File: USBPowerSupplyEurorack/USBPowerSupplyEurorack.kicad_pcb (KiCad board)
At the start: 2 copper layers, 9.8 x 110 mm, 23 parts, among them J1 1734366-1, J2 10129381-910001BLF, Q1 Q_PMOS_GSD, T1 RS6-0512D

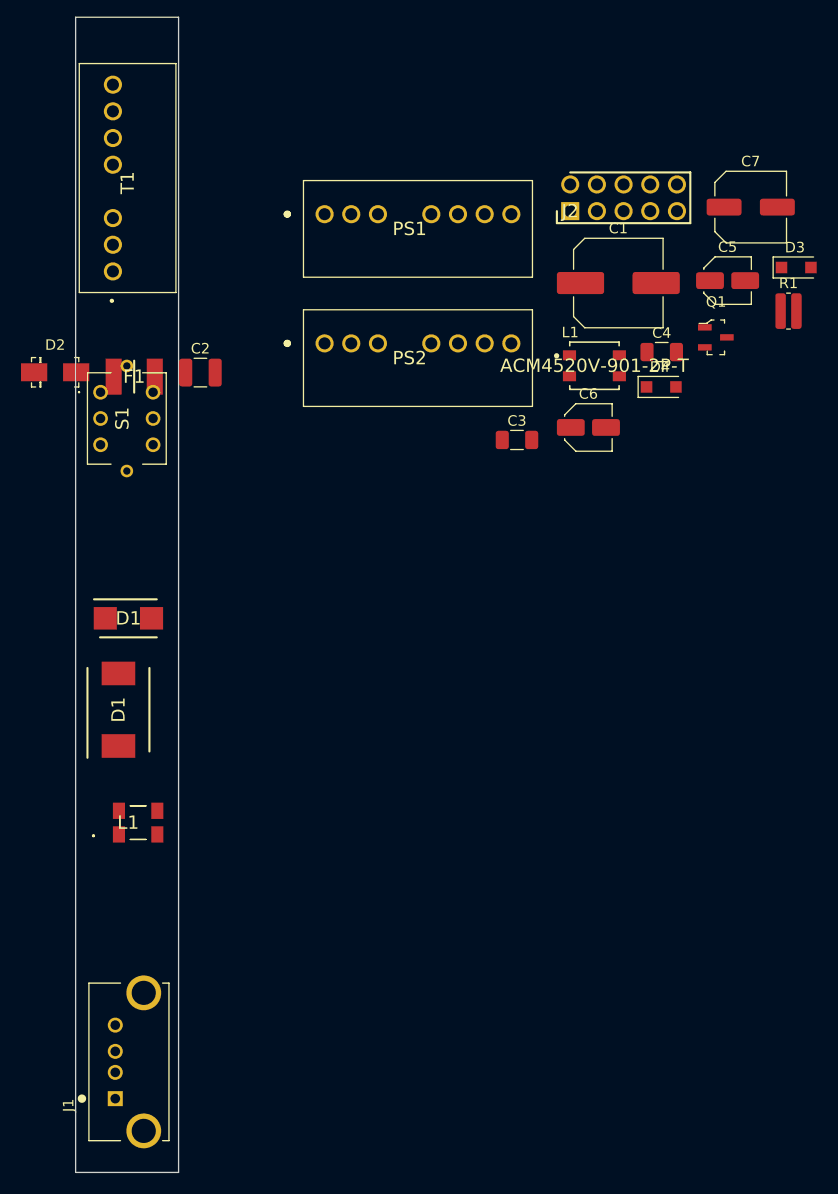
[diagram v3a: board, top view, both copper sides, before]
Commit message: updated all footprints in pcbnew
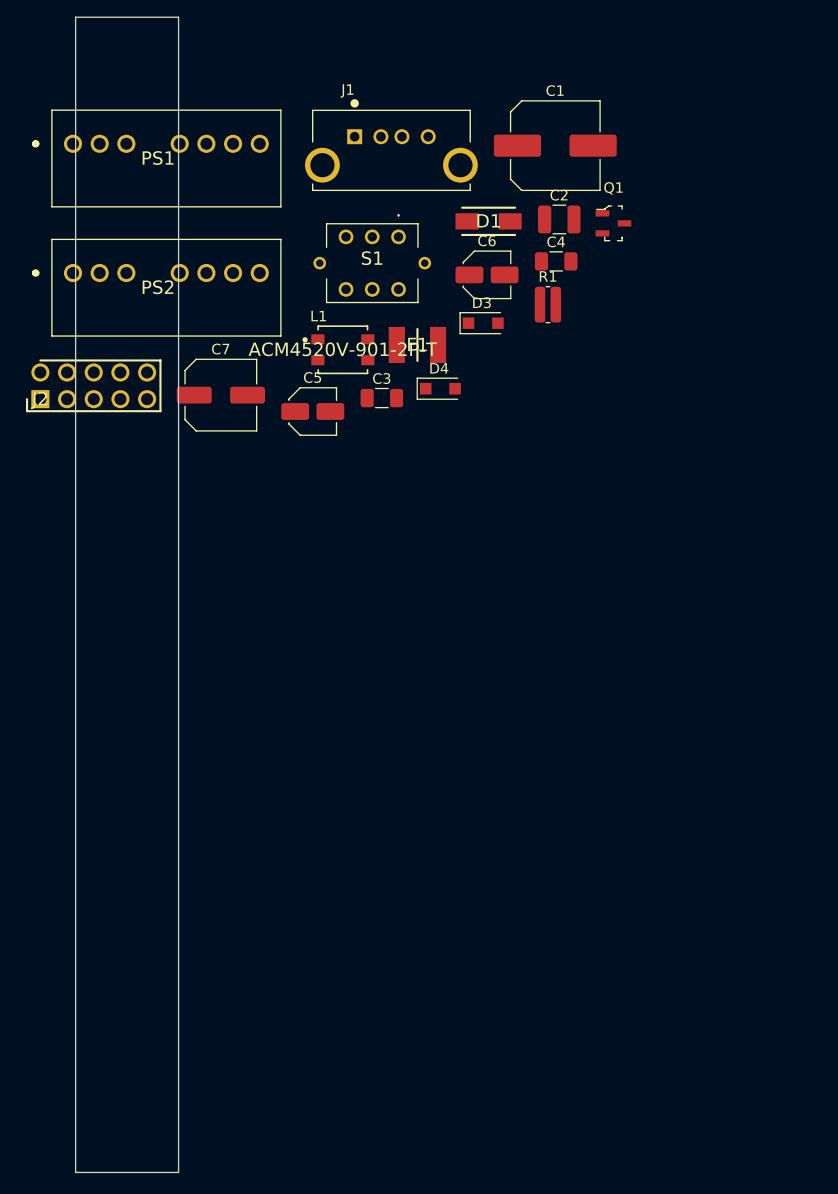
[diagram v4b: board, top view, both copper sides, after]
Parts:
- removed the D1 at (139.6, 105.3)
- removed the D1 at (138.6, 114.0)
- removed D2: SMAJ5.0CA, digikey-footprints:DO-214AC
- removed the L1 at (183.9, 81.3)
- removed the L1 at (140.5, 124.8)
- removed T1: RS6-0512D, RS6-0512D:RS60505S
- added D1: SMAJ5.0CA, DIONM5026X229N, F.Cu at (173.9, 67.6)
- added L1: ACM4520V-901-2P-T, eec2:TDK-ACM4520V-901-2P-T-0, F.Cu at (160.0, 79.8)
- moved J1 94.4 mm to (161.1, 59.5), turned to 0 degrees
- moved C7 53.5 mm to (148.4, 84.1)
- moved J2 53.5 mm to (131.2, 84.5)
- moved C5 41.4 mm to (157.1, 85.7)
- moved C2 37.1 mm to (180.6, 67.4)
- moved S1 32.0 mm to (165.3, 69.0), turned to 0 degrees
- moved D3 30.3 mm to (173.4, 77.3)
- moved F1 27.1 mm to (167.1, 79.3)
- moved PS1 24.9 mm to (134.3, 60.2)
- moved PS2 24.9 mm to (134.3, 72.5)
- moved R1 22.9 mm to (179.5, 75.5)
- moved D4 21.0 mm to (169.3, 83.5)
- moved C6 17.4 mm to (173.7, 72.7)
- moved Q1 14.6 mm to (185.8, 67.8)
- moved C1 14.4 mm to (180.2, 60.4)
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
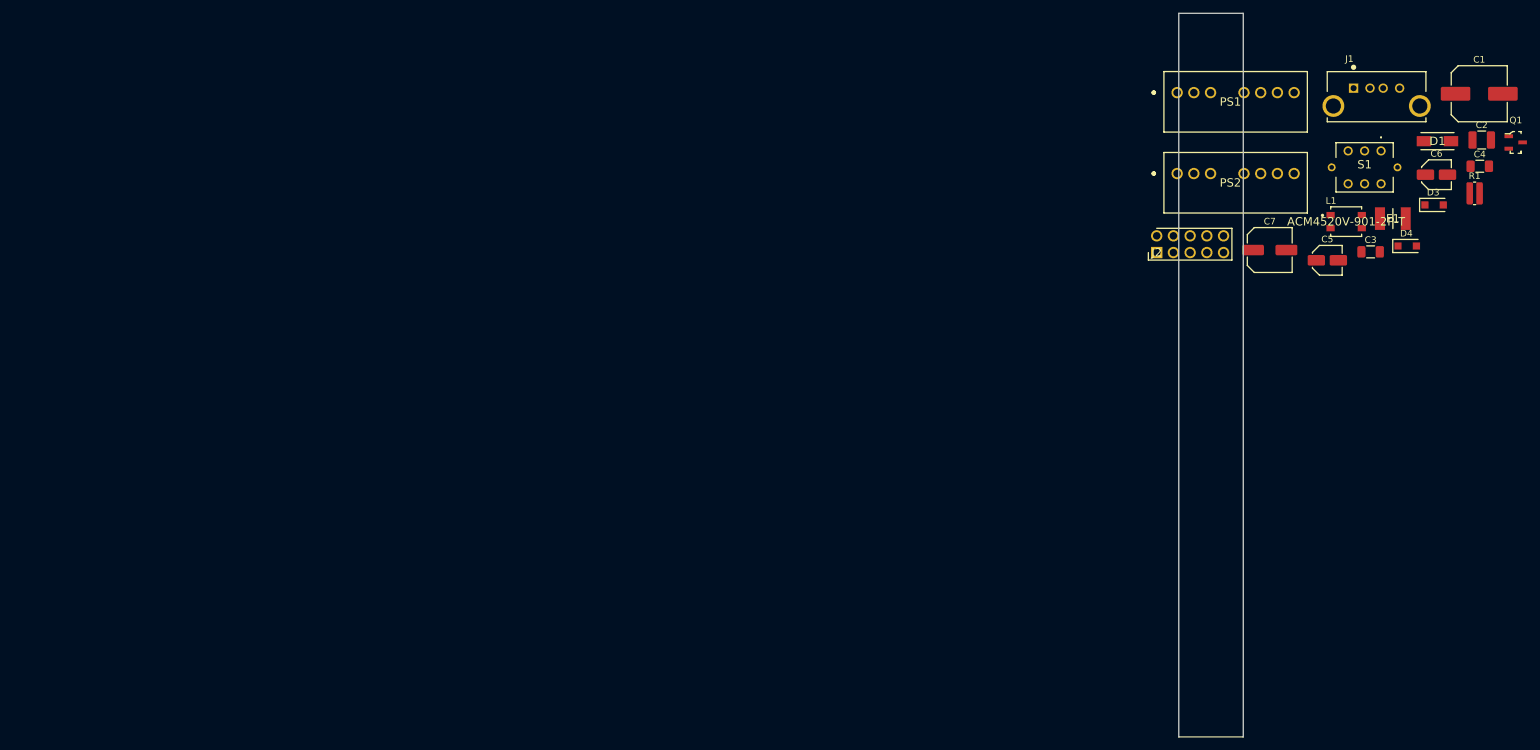
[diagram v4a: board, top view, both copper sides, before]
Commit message: placed components on the PCB
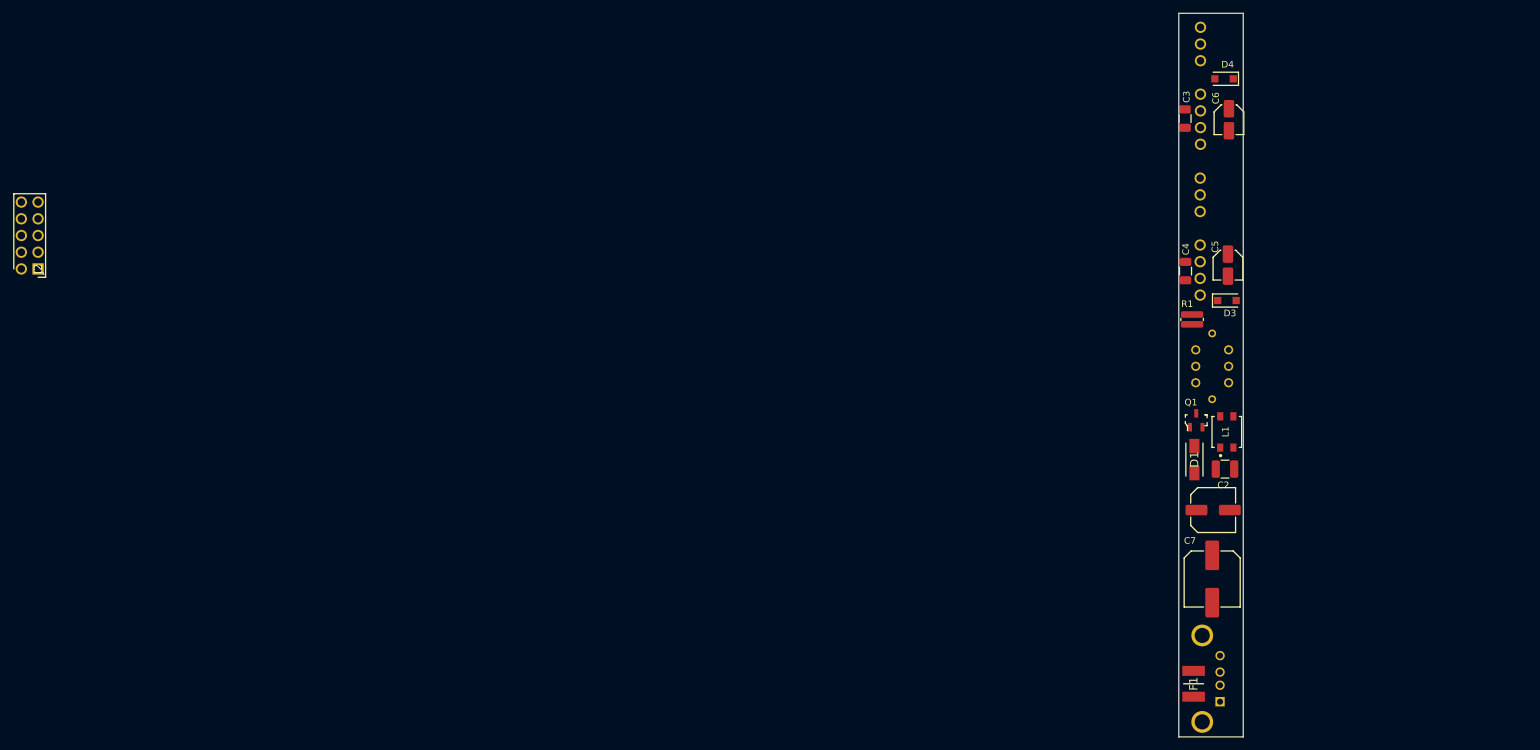
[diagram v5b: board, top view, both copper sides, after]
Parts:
- J1, PS1, PS2, S1: moved to B.Cu
- moved J2 170.0 mm to (-38.8, 87.0), turned to 90 degrees
- moved J1 95.4 mm to (140.8, 152.8), turned to 90 degrees
- moved C1 84.2 mm to (139.6, 134.1), turned to 270 degrees
- moved F1 76.9 mm to (136.8, 150.0), turned to 90 degrees
- moved Q1 64.3 mm to (137.2, 110.0), turned to 90 degrees
- moved C2 63.4 mm to (141.6, 117.4)
- moved D1 60.9 mm to (136.9, 116.0), turned to 90 degrees
- moved C4 47.5 mm to (135.6, 87.3), turned to 270 degrees
- moved R1 47.0 mm to (136.6, 94.7), turned to 90 degrees
- moved S1 45.1 mm to (137.1, 104.3), turned to 270 degrees
- moved C7 40.4 mm to (139.8, 123.6)
- moved D4 37.7 mm to (141.4, 58.1), turned to 180 degrees
- moved L1 36.8 mm to (141.8, 111.8), turned to 90 degrees
- moved C3 34.7 mm to (135.5, 64.1), turned to 270 degrees
- moved D3 34.7 mm to (141.9, 91.8)
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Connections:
- C1 pad 2: +5V -> GND
- C2 pad 2: +5V -> GND
- C7 pad 2: +5V -> GND
- D1 pad 2: +5V -> GND
- J1 pad 4: +5V -> GND
- L1 pad 2: +5V -> GND
- Q1 pad 1: +5V -> GND

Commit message: routing test for price evaluation
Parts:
- moved D4 12.0 mm to (141.9, 70.1)
- moved F1 1.38 mm to (136.8, 148.7)
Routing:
- net GND: track 0.00 -> 47.8 mm
- net +5VD: track 0.00 -> 46.4 mm
- net 0V: track 0.00 -> 27.0 mm
- net Net-(C1-Pad1): track 0.00 -> 24.9 mm
- net Net-(J1-PadSH1): track 0.00 -> 18.0 mm
- net -12V: track 0.00 -> 10.7 mm
- net +5V: track 0.00 -> 10.0 mm
- net +12V: track 0.00 -> 6.94 mm
- net Net-(F1-Pad1): track 0.00 -> 4.86 mm
- net Net-(R1-Pad1): track 0.00 -> 3.62 mm

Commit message: finished updating footprints, edited TVS diode's footprint
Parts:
- removed L1: ACM4520V-901-2P-T, eec2:TDK-ACM4520V-901-2P-T-0
- added FL1: ACP3225-102-2P-T000, ACP3225-102-2P-T000:ACP3225, F.Cu at (184.5, 85.4)
- C1: footprint Capacitor_SMD:C_Elec_8x10.2 -> Capacitor_SMD:C_Elec_6.3x7.7
- C2: value 22uFMLCC -> 22uF; footprint Capacitor_SMD:C_1210_3225Metric -> Capacitor_SMD:C_0805_2012Metric
- C3, C4: value 100nF MLCC -> 100nF; footprint Capacitor_SMD:C_1206_3216Metric -> Capacitor_SMD:C_0402_1005Metric
- C5, C6: value 1uF -> 4.7uF
- C7: footprint Capacitor_SMD:C_Elec_6.3x5.8 -> Capacitor_SMD:C_Elec_5x5.4
- D1: footprint DIONM5026X229N -> digikey-footprints:DO-214AC-BIPOLAR
- D3, D4: value 1N4004 -> 1N4007
- F1: footprint 1812L110_16DR:FUSC4632X125N -> Fuse:Fuse_1812_4532Metric
- J1, PS1, PS2, S1: moved to F.Cu
- R1: value 510 -> 1.5K; footprint Resistor_SMD:R_0612_1632Metric -> Resistor_SMD:R_0805_2012Metric
- moved J2 192.1 mm to (153.2, 86.3), turned to 0 degrees
- moved J1 100.8 mm to (183.2, 61.3), turned to 0 degrees
- moved F1 85.5 mm to (189.2, 81.1), turned to 0 degrees
- moved Q1 75.4 mm to (201.9, 71.2), turned to 0 degrees
- moved C3 71.0 mm to (206.5, 66.3), turned to 0 degrees
- moved D1 67.5 mm to (201.2, 95.5), turned to 0 degrees
- moved C2 66.4 mm to (194.9, 77.8)
- moved C4 64.6 mm to (198.9, 74.6), turned to 0 degrees
- moved D4 60.5 mm to (202.3, 67.0), turned to 0 degrees
- moved S1 60.3 mm to (187.3, 70.8), turned to 0 degrees
- moved C1 59.0 mm to (183.7, 94.9), turned to 0 degrees
- moved C5 56.2 mm to (195.8, 70.1), turned to 0 degrees
- moved D3 55.6 mm to (194.8, 74.7)
- moved R1 53.3 mm to (189.0, 85.0), turned to 0 degrees
- moved C7 48.7 mm to (169.7, 85.2)
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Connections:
- C3 pad 1: 0V -> +12V
- C3 pad 2: -12V -> 0V
- C4 pad 1: +12V -> 0V
- C4 pad 2: 0V -> -12V
- F1 pad 2: +5VD -> +5V
- PS1 pad 3: Net-(PS1-Pad3) -> CTRL
- PS2 pad 3: Net-(PS2-Pad3) -> CTRL
- S1 pad 1: +5VD -> CTRL
- S1 pad 2: +5VD -> CTRL
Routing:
- net GND: track 47.8 -> 0.00 mm
- net +5VD: track 46.4 -> 0.00 mm
- net 0V: track 27.0 -> 0.00 mm
- net Net-(C1-Pad1): track 24.9 -> 0.00 mm
- net Net-(J1-PadSH1): track 18.0 -> 0.00 mm
- net -12V: track 10.7 -> 0.00 mm
- net +5V: track 10.0 -> 0.00 mm
- net +12V: track 6.94 -> 0.00 mm
- net Net-(F1-Pad1): track 4.86 -> 0.00 mm
- net Net-(R1-Pad1): track 3.62 -> 0.00 mm

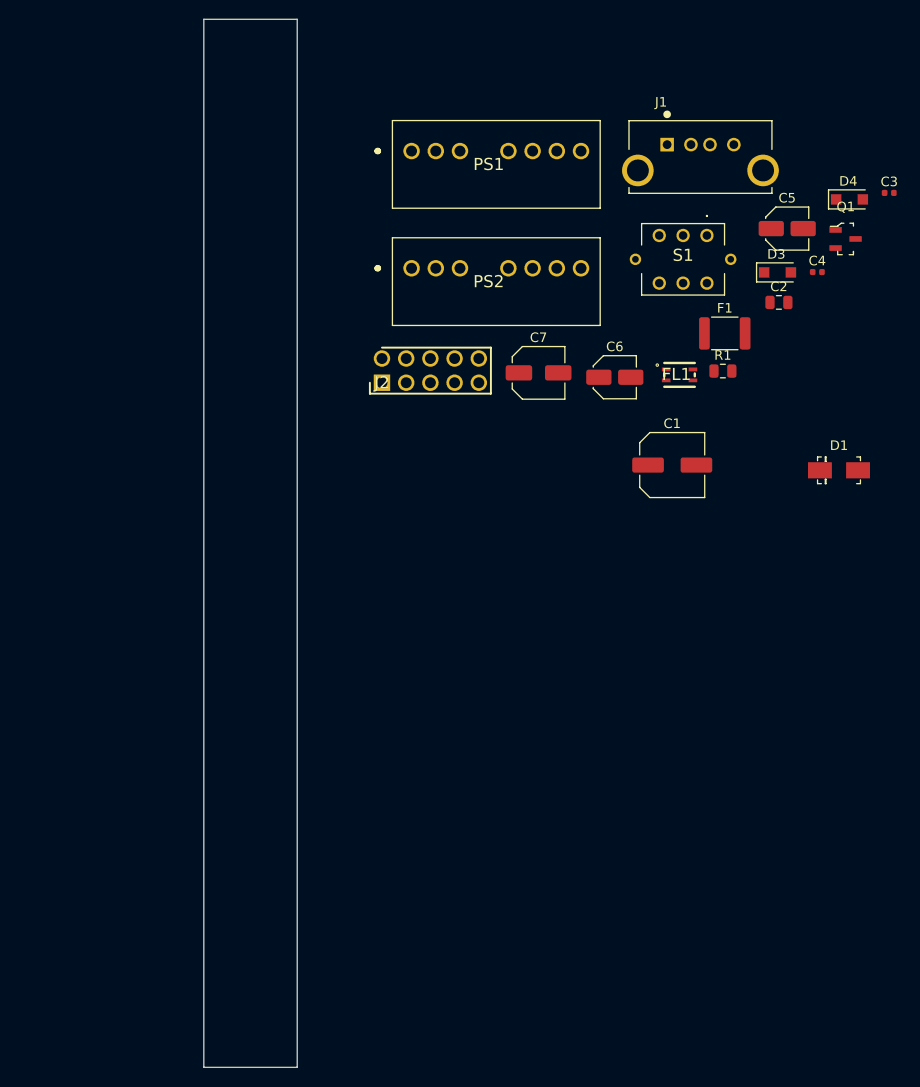
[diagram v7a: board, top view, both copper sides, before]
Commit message: placed components, need to change power 2x5 for SMT
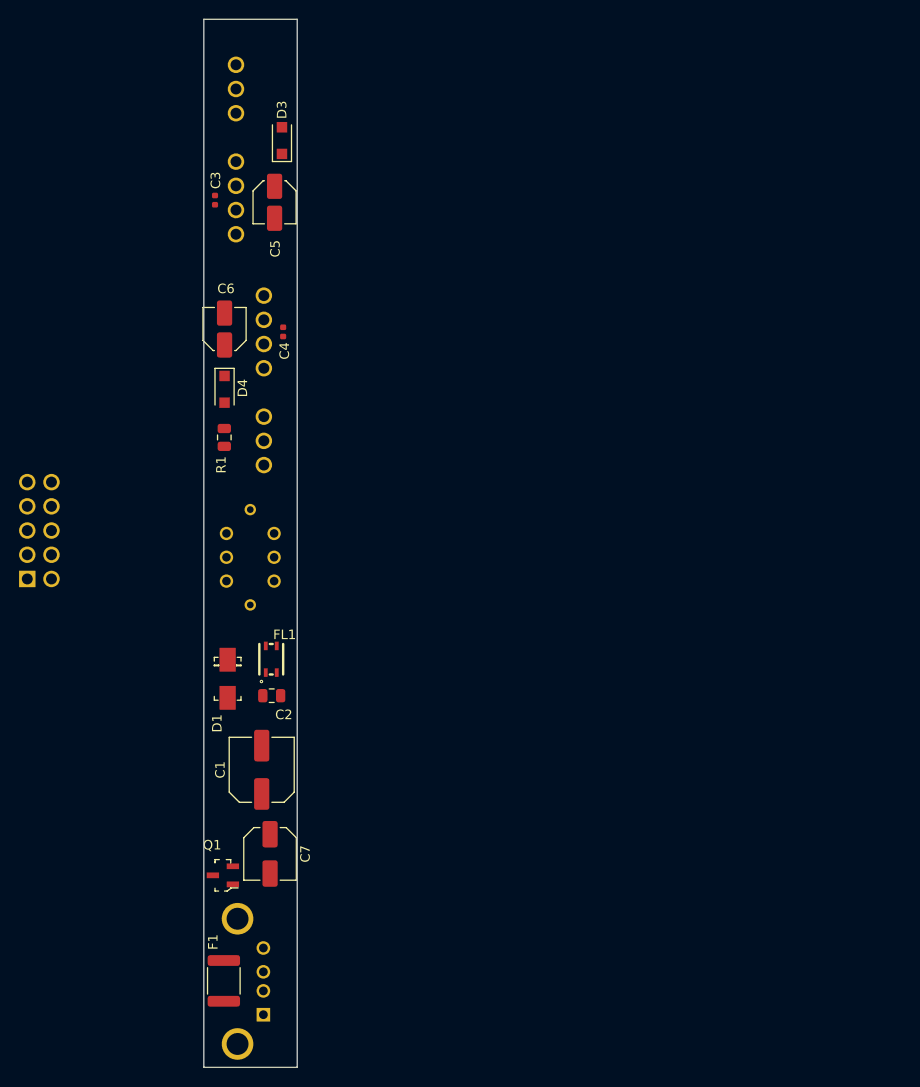
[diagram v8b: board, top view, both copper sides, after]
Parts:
- J1, J2, PS1, PS2, S1: moved to B.Cu
- moved J1 100.7 mm to (140.8, 152.6), turned to 90 degrees
- moved Q1 93.4 mm to (136.6, 137.9), turned to 180 degrees
- moved F1 85.9 mm to (136.7, 149.0), turned to 90 degrees
- moved C3 70.8 mm to (135.7, 67.1), turned to 270 degrees
- moved D4 68.5 mm to (136.7, 87.0), turned to 270 degrees
- moved D1 67.8 mm to (137.1, 117.3), turned to 270 degrees
- moved C2 67.3 mm to (141.7, 119.1)
- moved S1 62.1 mm to (136.9, 107.1), turned to 270 degrees
- moved C7 57.8 mm to (141.5, 135.7), turned to 270 degrees
- moved C4 56.4 mm to (142.9, 80.9), turned to 90 degrees
- moved C5 53.9 mm to (142.0, 67.3), turned to 270 degrees
- moved D3 53.8 mm to (142.8, 60.9), turned to 90 degrees
- moved C1 53.6 mm to (140.6, 126.9), turned to 90 degrees
- moved R1 52.8 mm to (136.7, 92.0), turned to 90 degrees
- moved FL1 52.2 mm to (141.6, 115.3), turned to 90 degrees
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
